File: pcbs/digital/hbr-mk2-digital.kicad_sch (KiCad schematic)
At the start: 98 parts, among them J1 Conn_01x09, J10 Conn_01x06, J11 Conn_01x05, J12 Conn_01x02, J13 Conn_01x02, J14 Conn_01x02, J2 Conn_01x02, J3 Conn_01x04, J4 Conn_01x04, J5 Conn_01x03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

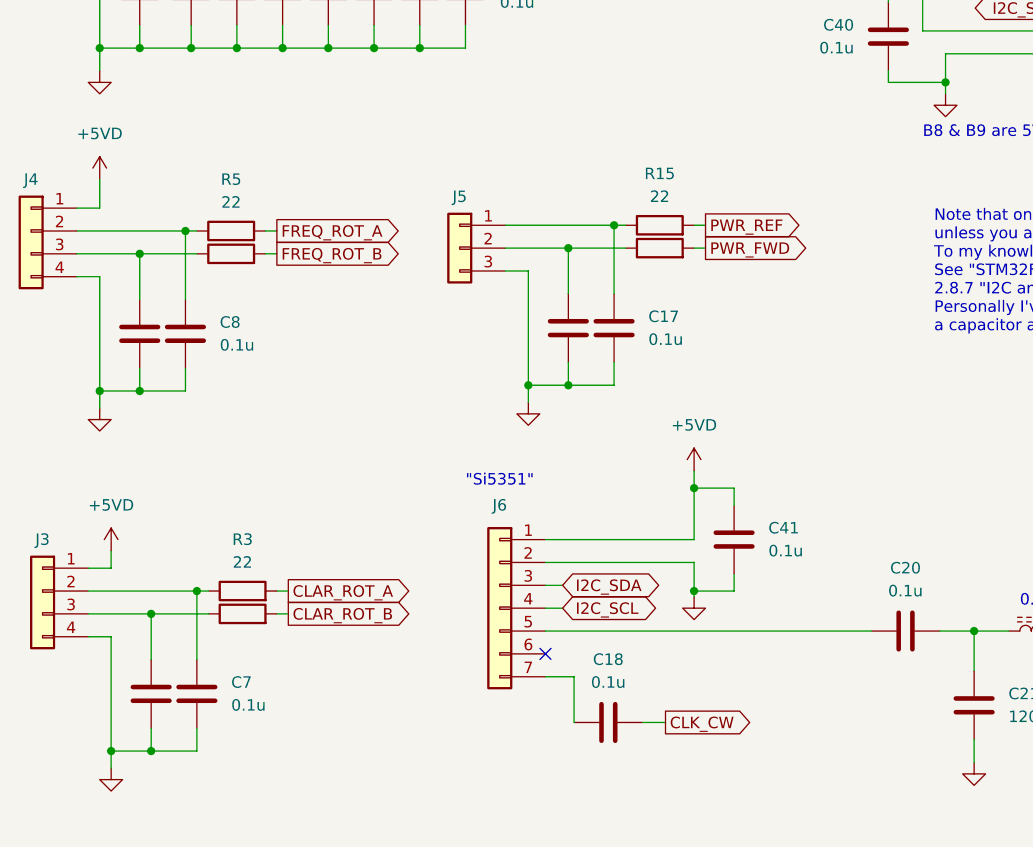
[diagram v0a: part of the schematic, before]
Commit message: Mark C3,C4,C7,C8 as DNP
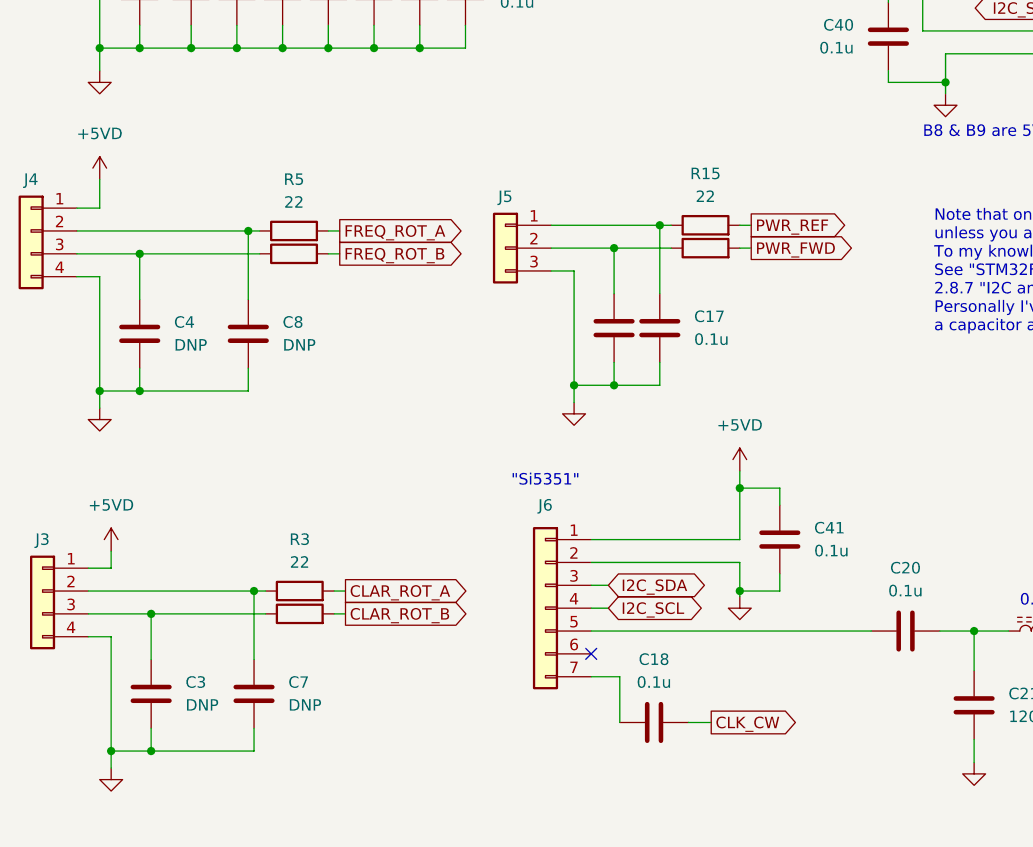
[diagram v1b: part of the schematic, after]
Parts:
- C3, C4, C7, C8: value 0.1u -> DNP
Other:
- moved on the sheet: C17, C18, C41, C7, C8, J5, J6, R15, R3, R5
